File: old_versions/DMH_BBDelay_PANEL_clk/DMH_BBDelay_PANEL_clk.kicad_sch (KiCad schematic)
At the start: 39 parts, among them J0 Panel_GND_Solder_Wire_Pad

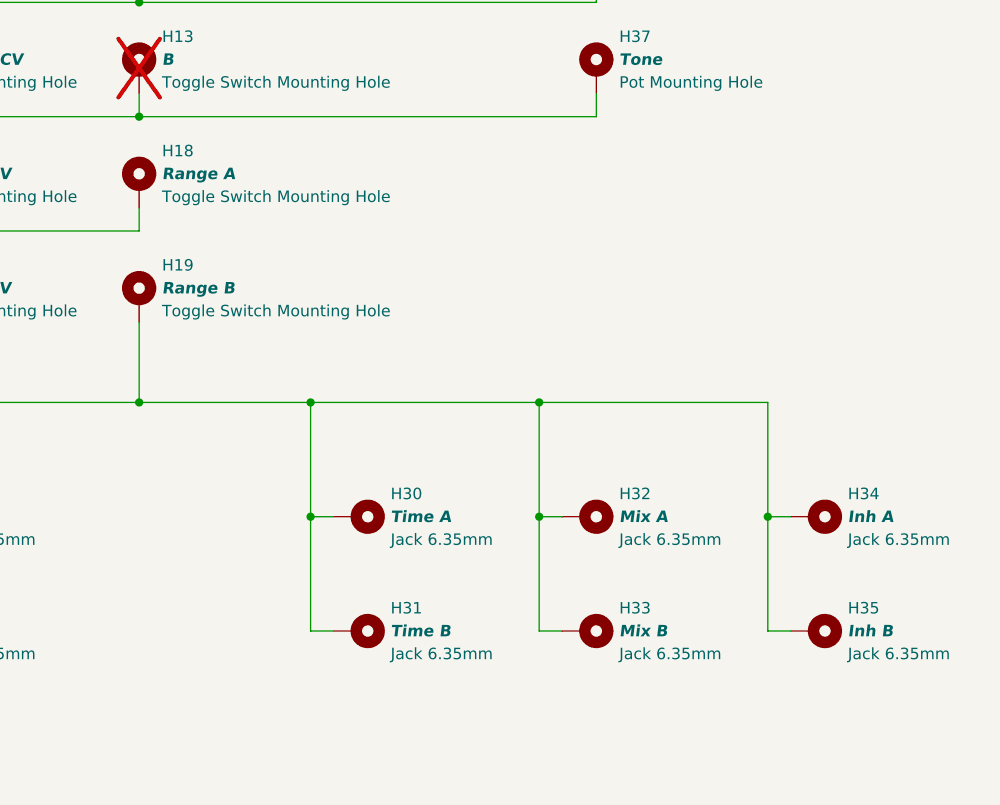
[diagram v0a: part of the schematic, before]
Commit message: Replaced Clock Sync with Inhibit input and Range
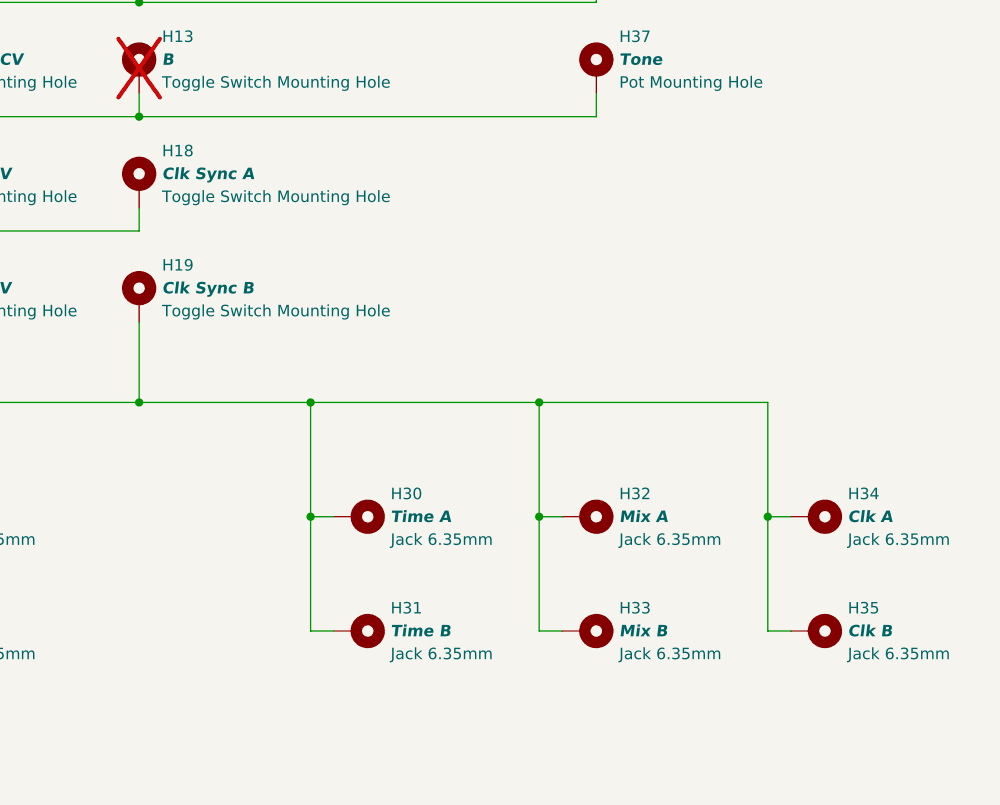
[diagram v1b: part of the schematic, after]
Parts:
- H18: value Range A -> Clk Sync A
- H19: value Range B -> Clk Sync B
- H34: value Inh A -> Clk A
- H35: value Inh B -> Clk B
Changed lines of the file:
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@@
 		)
 		(instances
-			(project "DMH_BBDelay_PANEL"
+			(project "DMH_BBDelay_PANEL_clk"
 				(path "/a552705f-a9fe-462e-9913-5cfcc08b233c"
 					(reference "H30")
@@
 		)
 		(instances
-			(project "DMH_BBDelay_PANEL"
+			(project "DMH_BBDelay_PANEL_clk"
 				(path "/a552705f-a9fe-462e-9913-5cfcc08b233c"
 					(reference "H7")
@@
 		)
 		(instances
-			(project "DMH_BBDelay_PANEL"
+			(project "DMH_BBDelay_PANEL_clk"
 				(path "/a552705f-a9fe-462e-9913-5cfcc08b233c"
 					(reference "H2")
@@
 		)
 		(instances
-			(project "DMH_BBDelay_PANEL"
+			(project "DMH_BBDelay_PANEL_clk"
 				(path "/a552705f-a9fe-462e-9913-5cfcc08b233c"
 					(reference "H24")
@@
 		)
 		(instances
-			(project "DMH_BBDelay_PANEL"
+			(project "DMH_BBDelay_PANEL_clk"
 				(path "/a552705f-a9fe-462e-9913-5cfcc08b233c"
 					(reference "H12")
@@
 		)
 		(instances
-			(project "DMH_BBDelay_PANEL"
+			(project "DMH_BBDelay_PANEL_clk"
 				(path "/a552705f-a9fe-462e-9913-5cfcc08b233c"
 					(reference "H5")
@@
 		)
 		(instances
-			(project "DMH_BBDelay_PANEL"
+			(project "DMH_BBDelay_PANEL_clk"
 				(path "/a552705f-a9fe-462e-9913-5cfcc08b233c"
 					(reference "H20")
@@
 		)
 		(instances
-			(project "DMH_BBDelay_PANEL"
+			(project "DMH_BBDelay_PANEL_clk"
 				(path "/a552705f-a9fe-462e-9913-5cfcc08b233c"
 					(reference "H37")
@@
 		)
 		(instances
-			(project "DMH_BBDelay_PANEL"
+			(project "DMH_BBDelay_PANEL_clk"
 				(path "/a552705f-a9fe-462e-9913-5cfcc08b233c"
 					(reference "H36")
@@
 		)
 		(instances
-			(project "DMH_BBDelay_PANEL"
+			(project "DMH_BBDelay_PANEL_clk"
 				(path "/a552705f-a9fe-462e-9913-5cfcc08b233c"
 					(reference "H26")
@@
 		)
 		(instances
-			(project "DMH_BBDelay_PANEL"
+			(project "DMH_BBDelay_PANEL_clk"
 				(path "/a552705f-a9fe-462e-9913-5cfcc08b233c"
 					(reference "H29")
@@
 		)
 		(instances
-			(project "DMH_BBDelay_PANEL"
+			(project "DMH_BBDelay_PANEL_clk"
 				(path "/a552705f-a9fe-462e-9913-5cfcc08b233c"
 					(reference "H15")
@@
 		)
 		(instances
-			(project "DMH_BBDelay_PANEL"
+			(project "DMH_BBDelay_PANEL_clk"
 				(path "/a552705f-a9fe-462e-9913-5cfcc08b233c"
 					(reference "H13")
@@
 		)
 		(instances
-			(project "DMH_BBDelay_PANEL"
+			(project "DMH_BBDelay_PANEL_clk"
 				(path "/a552705f-a9fe-462e-9913-5cfcc08b233c"
 					(reference "H10")
@@
 		)
 		(instances
-			(project "DMH_BBDelay_PANEL"
+			(project "DMH_BBDelay_PANEL_clk"
 				(path "/a552705f-a9fe-462e-9913-5cfcc08b233c"
 					(reference "#PWR01")
@@
 		)
 		(instances
-			(project "DMH_BBDelay_PANEL"
+			(project "DMH_BBDelay_PANEL_clk"
 				(path "/a552705f-a9fe-462e-9913-5cfcc08b233c"
 					(reference "H6")
@@
 		)
 		(instances
-			(project "DMH_BBDelay_PANEL"
+			(project "DMH_BBDelay_PANEL_clk"
 				(path "/a552705f-a9fe-462e-9913-5cfcc08b233c"
 					(reference "H33")
@@
 		)
 		(instances
-			(project "DMH_BBDelay_PANEL"
+			(project "DMH_BBDelay_PANEL_clk"
 				(path "/a552705f-a9fe-462e-9913-5cfcc08b233c"
 					(reference "H21")
@@
 		)
 		(instances
-			(project "DMH_BBDelay_PANEL"
+			(project "DMH_BBDelay_PANEL_clk"
 				(path "/a552705f-a9fe-462e-9913-5cfcc08b233c"
 					(reference "H32")
@@
 		)
 		(instances
-			(project "DMH_BBDelay_PANEL"
+			(project "DMH_BBDelay_PANEL_clk"
 				(path "/a552705f-a9fe-462e-9913-5cfcc08b233c"
 					(reference "H9")
@@
 		)
 		(instances
-			(project "DMH_BBDelay_PANEL"
+			(project "DMH_BBDelay_PANEL_clk"
 				(path "/a552705f-a9fe-462e-9913-5cfcc08b233c"
 					(reference "H31")
@@
 		)
 		(instances
-			(project "DMH_BBDelay_PANEL"
+			(project "DMH_BBDelay_PANEL_clk"
 				(path "/a552705f-a9fe-462e-9913-5cfcc08b233c"
 					(reference "H23")
@@
 		)
 		(instances
-			(project "DMH_BBDelay_PANEL"
+			(project "DMH_BBDelay_PANEL_clk"
 				(path "/a552705f-a9fe-462e-9913-5cfcc08b233c"
 					(reference "H27")
@@
 		)
 		(instances
-			(project "DMH_BBDelay_PANEL"
+			(project "DMH_BBDelay_PANEL_clk"
 				(path "/a552705f-a9fe-462e-9913-5cfcc08b233c"
 					(reference "H8")
@@
 		)
 		(instances
-			(project "DMH_BBDelay_PANEL"
+			(project "DMH_BBDelay_PANEL_clk"
 				(path "/a552705f-a9fe-462e-9913-5cfcc08b233c"
 					(reference "H3")
@@
 		)
 		(instances
-			(project "DMH_BBDelay_PANEL"
+			(project "DMH_BBDelay_PANEL_clk"
 				(path "/a552705f-a9fe-462e-9913-5cfcc08b233c"
 					(reference "H14")
@@
 		)
 		(instances
-			(project "DMH_BBDelay_PANEL"
+			(project "DMH_BBDelay_PANEL_clk"
 				(path "/a552705f-a9fe-462e-9913-5cfcc08b233c"
 					(reference "H11")
@@
 		)
 		(instances
-			(project "DMH_BBDelay_PANEL"
+			(project "DMH_BBDelay_PANEL_clk"
 				(path "/a552705f-a9fe-462e-9913-5cfcc08b233c"
 					(reference "H38")
@@
 		)
 		(instances
-			(project "DMH_BBDelay_PANEL"
+			(project "DMH_BBDelay_PANEL_clk"
 				(path "/a552705f-a9fe-462e-9913-5cfcc08b233c"
 					(reference "H28")
@@
 		)
 		(instances
-			(project "DMH_BBDelay_PANEL"
+			(project "DMH_BBDelay_PANEL_clk"
 				(path "/a552705f-a9fe-462e-9913-5cfcc08b233c"
 					(reference "H25")
@@
 			)
 		)
-		(property "Value" "Range B"
+		(property "Value" "Clk Sync B"
 			(at 104.14 88.9 0)
 			(show_name no)
@@
 		)
 		(instances
-			(project "DMH_BBDelay_PANEL"
+			(project "DMH_BBDelay_PANEL_clk"
 				(path "/a552705f-a9fe-462e-9913-5cfcc08b233c"
 					(reference "H19")
@@
 		)
 		(instances
-			(project "DMH_BBDelay_PANEL"
+			(project "DMH_BBDelay_PANEL_clk"
 				(path "/a552705f-a9fe-462e-9913-5cfcc08b233c"
 					(reference "H22")
@@
 			)
 		)
-		(property "Value" "Range A"
+		(property "Value" "Clk Sync A"
 			(at 104.14 76.2 0)
 			(show_name no)
@@
 		)
 		(instances
-			(project "DMH_BBDelay_PANEL"
+			(project "DMH_BBDelay_PANEL_clk"
 				(path "/a552705f-a9fe-462e-9913-5cfcc08b233c"
 					(reference "H18")
@@
 		)
 		(instances
-			(project "DMH_BBDelay_PANEL"
+			(project "DMH_BBDelay_PANEL_clk"
 				(path "/a552705f-a9fe-462e-9913-5cfcc08b233c"
 					(reference "H17")
@@
 			)
 		)
-		(property "Value" "Inh B"
+		(property "Value" "Clk B"
 			(at 180.34 127 0)
 			(show_name no)
@@
 		)
 		(instances
-			(project "DMH_BBDelay_PANEL"
+			(project "DMH_BBDelay_PANEL_clk"
 				(path "/a552705f-a9fe-462e-9913-5cfcc08b233c"
 					(reference "H35")
@@
 			)
 		)
-		(property "Value" "Inh A"
+		(property "Value" "Clk A"
 			(at 180.34 114.3 0)
 			(show_name no)
@@
 		)
 		(instances
-			(project "DMH_BBDelay_PANEL"
+			(project "DMH_BBDelay_PANEL_clk"
 				(path "/a552705f-a9fe-462e-9913-5cfcc08b233c"
 					(reference "H34")
@@
 		)
 		(instances
-			(project "DMH_BBDelay_PANEL"
+			(project "DMH_BBDelay_PANEL_clk"
 				(path "/a552705f-a9fe-462e-9913-5cfcc08b233c"
 					(reference "H4")
@@
 		)
 		(instances
-			(project "DMH_BBDelay_PANEL"
+			(project "DMH_BBDelay_PANEL_clk"
 				(path "/a552705f-a9fe-462e-9913-5cfcc08b233c"
 					(reference "J0")
@@
 		)
 		(instances
-			(project "DMH_BBDelay_PANEL"
+			(project "DMH_BBDelay_PANEL_clk"
 				(path "/a552705f-a9fe-462e-9913-5cfcc08b233c"
 					(reference "H1")
@@
 		)
 		(instances
-			(project "DMH_BBDelay_PANEL"
+			(project "DMH_BBDelay_PANEL_clk"
 				(path "/a552705f-a9fe-462e-9913-5cfcc08b233c"
 					(reference "H16")
